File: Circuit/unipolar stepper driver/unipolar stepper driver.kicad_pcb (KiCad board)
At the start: 2 copper layers, 78.7 x 43.2 mm, 20 parts, among them Q1 S8050, Q2 S8050, Q3 S8050, Q4 S8050

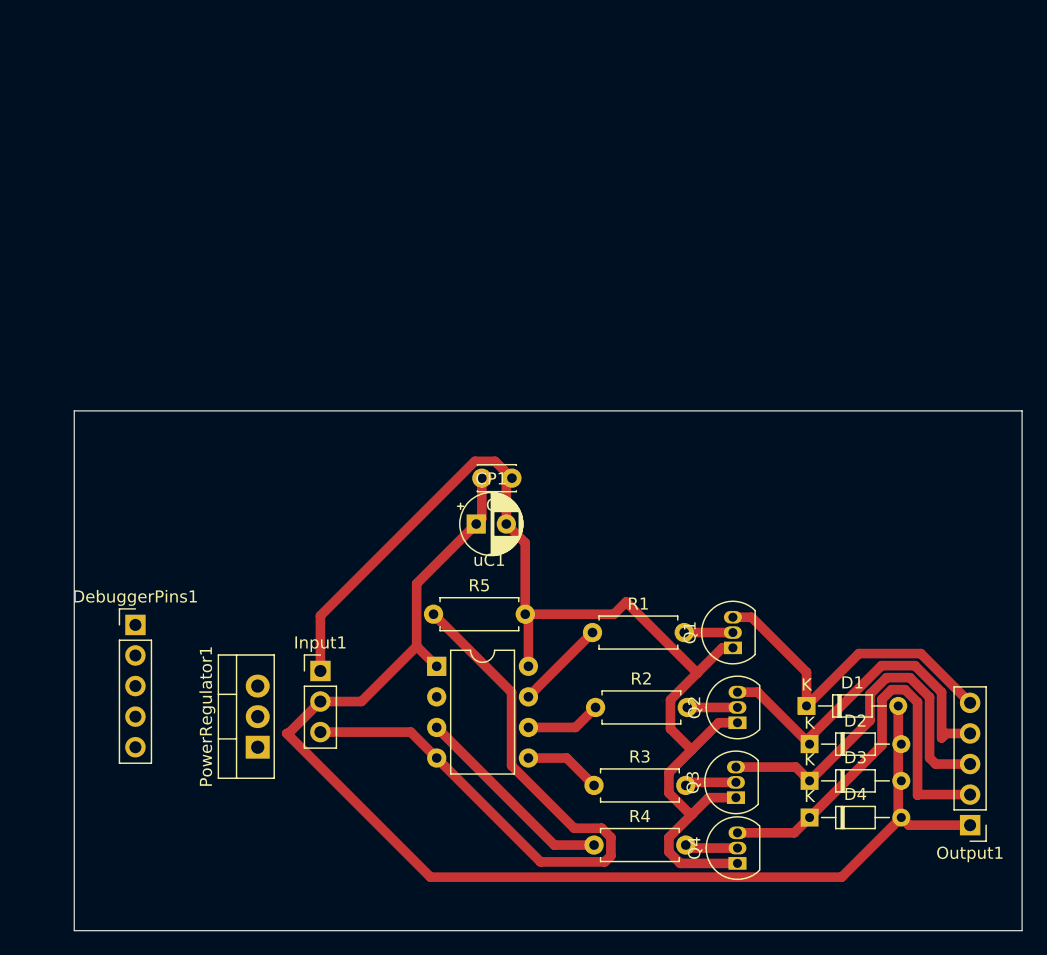
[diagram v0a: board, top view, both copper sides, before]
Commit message: Created Unipolar Stepper PCB design
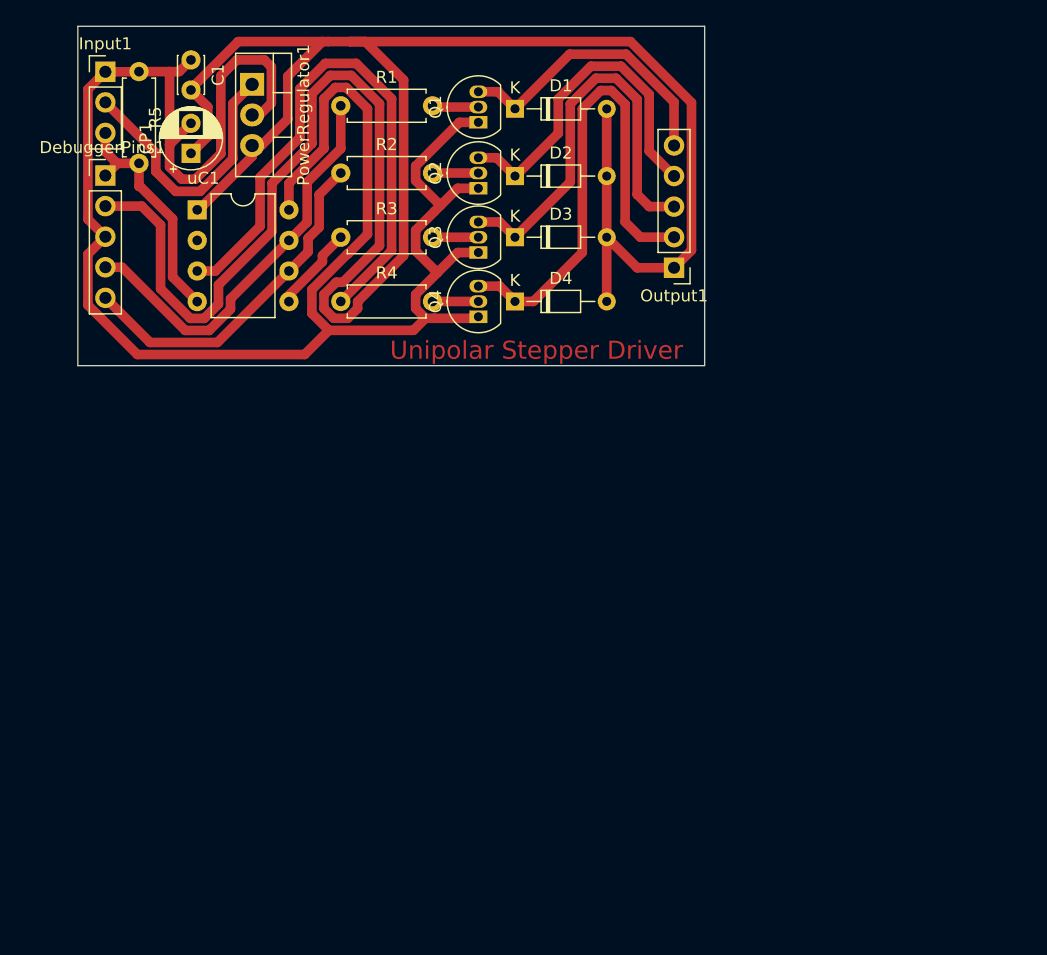
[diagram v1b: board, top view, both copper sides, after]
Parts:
- moved D1 55.2 mm to (49.0, -12.4)
- moved PowerRegulator1 55.1 mm to (27.2, -14.5), turned to -90 degrees
- moved D2 53.2 mm to (49.0, -6.86)
- moved Input1 52.9 mm to (15.0, -15.5)
- moved Output1 52.4 mm to (62.2, 0.76)
- moved D3 51.4 mm to (49.0, -1.78)
- moved R5 51.3 mm to (17.8, -15.5), turned to -90 degrees
- moved Q4 50.3 mm to (46.0, 4.83)
- moved R3 50.2 mm to (34.5, -1.78)
- moved Q3 50.1 mm to (46.0, -0.51)
- moved R4 49.8 mm to (34.5, 3.56)
- moved D4 49.4 mm to (49.0, 3.56)
- moved Q2 49.3 mm to (46.0, -5.84)
- moved R2 49.2 mm to (34.5, -7.11)
- moved Q1 48.5 mm to (46.0, -11.3)
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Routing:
- net +5V: track 105.8 -> 201.1 mm
- net GND: track 98.3 -> 163.5 mm
- net Control_Input: track 56.3 -> 19.7 mm
- net Coil_4: track 17.1 -> 47.8 mm
- net Coil_1: track 7.55 -> 34.0 mm
- net Coil_2: track 6.27 -> 29.2 mm
- net +12V: track 0.00 -> 22.5 mm
- net Net-(D4-Pad1): track 34.7 -> 41.8 mm
- net Net-(D3-Pad1): track 31.0 -> 35.1 mm
- net Net-(D1-Pad1): track 27.9 -> 24.0 mm
- net Coil_3: track 6.39 -> 7.13 mm
- net Net-(Q4-Pad2): track 4.40 -> 3.81 mm
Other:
- board size 78.7 x 43.2 mm -> 52.1 x 28.2 mm
- board text added: "Unipolar Stepper Driver"

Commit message: Fixed numerous bugs in CAM module and marked numerous others
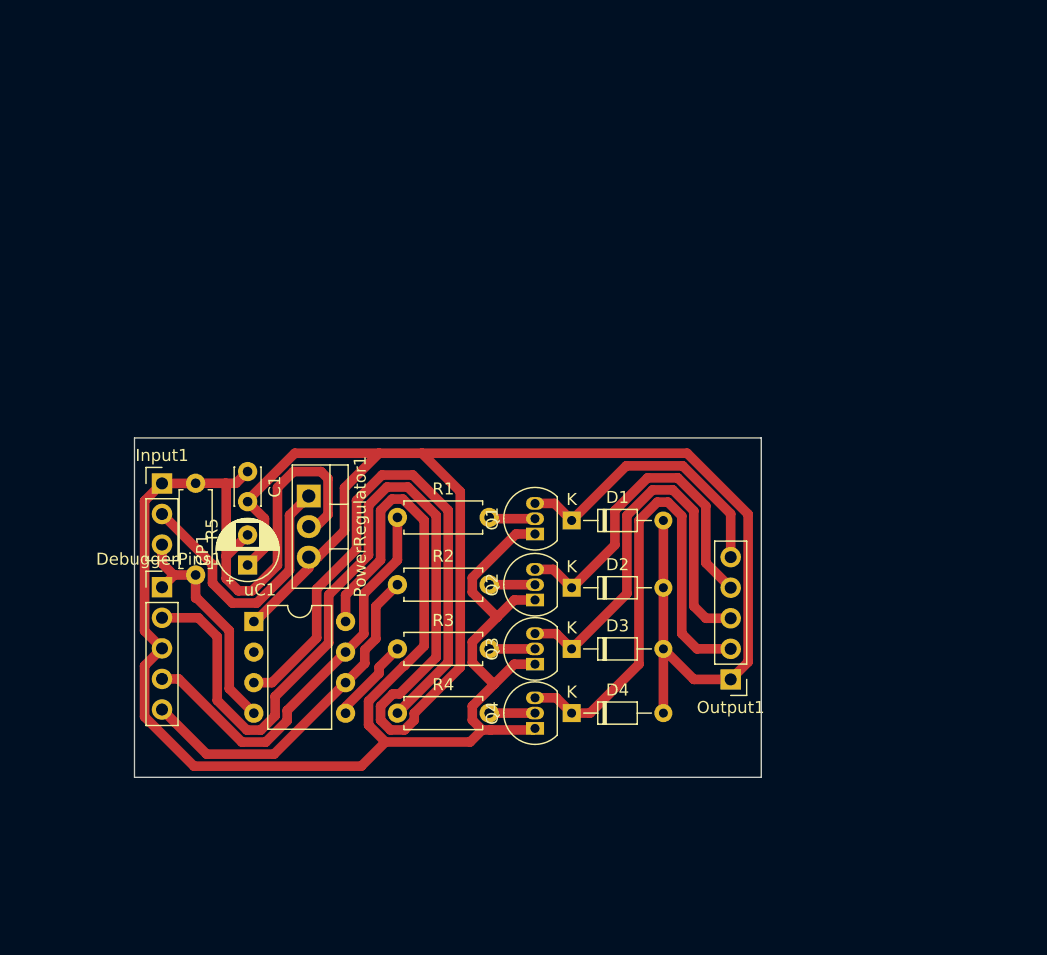
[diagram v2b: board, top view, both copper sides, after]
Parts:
- moved D4 34.5 mm to (53.7, 37.8)
- moved DebuggerPins1 34.5 mm to (19.7, 27.3)
- moved Output1 34.5 mm to (66.9, 35.0)
- moved Q1 34.5 mm to (50.7, 22.9)
- moved Q2 34.5 mm to (50.7, 28.4)
- moved Q3 34.5 mm to (50.7, 33.7)
- moved R2 34.5 mm to (39.2, 27.1)
- moved R4 34.5 mm to (39.2, 37.8)
- moved uC1 34.5 mm to (27.3, 30.1)
- moved C1 34.5 mm to (26.8, 17.7)
- moved CP1 34.5 mm to (26.8, 25.5)
- moved D1 34.5 mm to (53.7, 21.8)
- moved D2 34.5 mm to (53.7, 27.3)
- moved D3 34.5 mm to (53.7, 32.4)
- moved Input1 34.5 mm to (19.7, 18.7)
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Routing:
- net +5V: track 201.1 -> 199.9 mm
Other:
- board text removed: "Unipolar Stepper Driver"

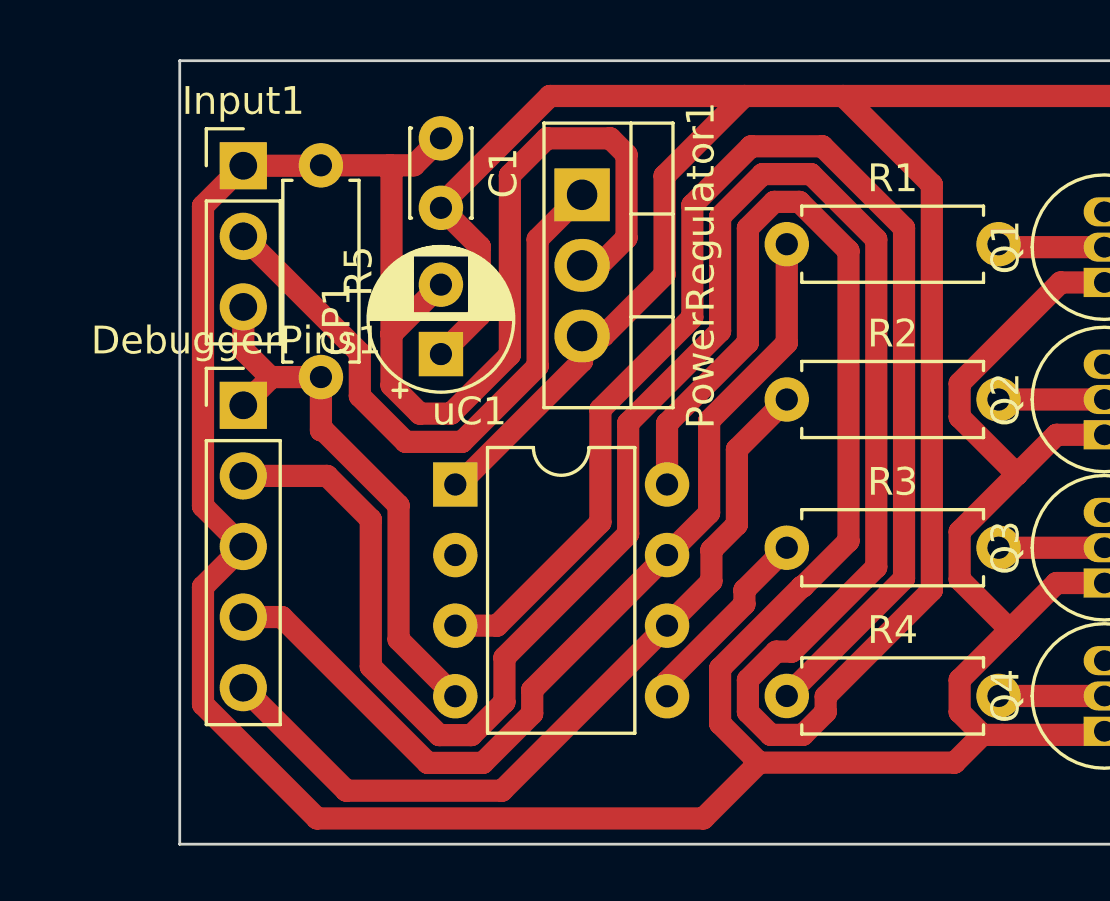
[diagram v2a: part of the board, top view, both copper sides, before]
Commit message: unipolar circuit development
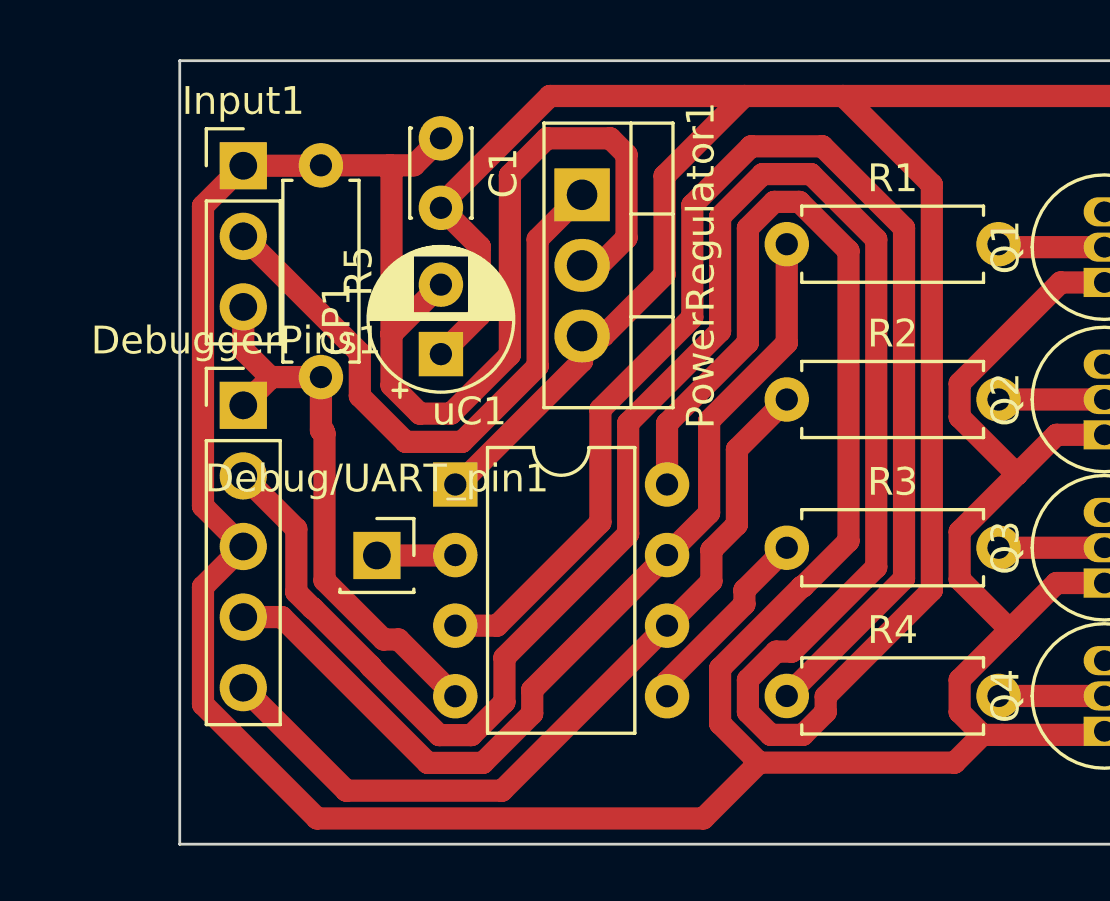
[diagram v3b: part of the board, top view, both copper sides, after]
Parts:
- added Debug/UART_pin1: Conn_01x01_Socket, Connector_PinSocket_2.54mm:PinSocket_1x01_P2.54mm_Vertical, F.Cu at (24.5, 32.7)
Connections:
- uC1 pad 2: unconnected-(uC1-Pad2) -> Debug/UART pin
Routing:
- net Debug/UART pin: track 0.00 -> 2.83 mm
- net +5V: track 199.9 -> 198.9 mm

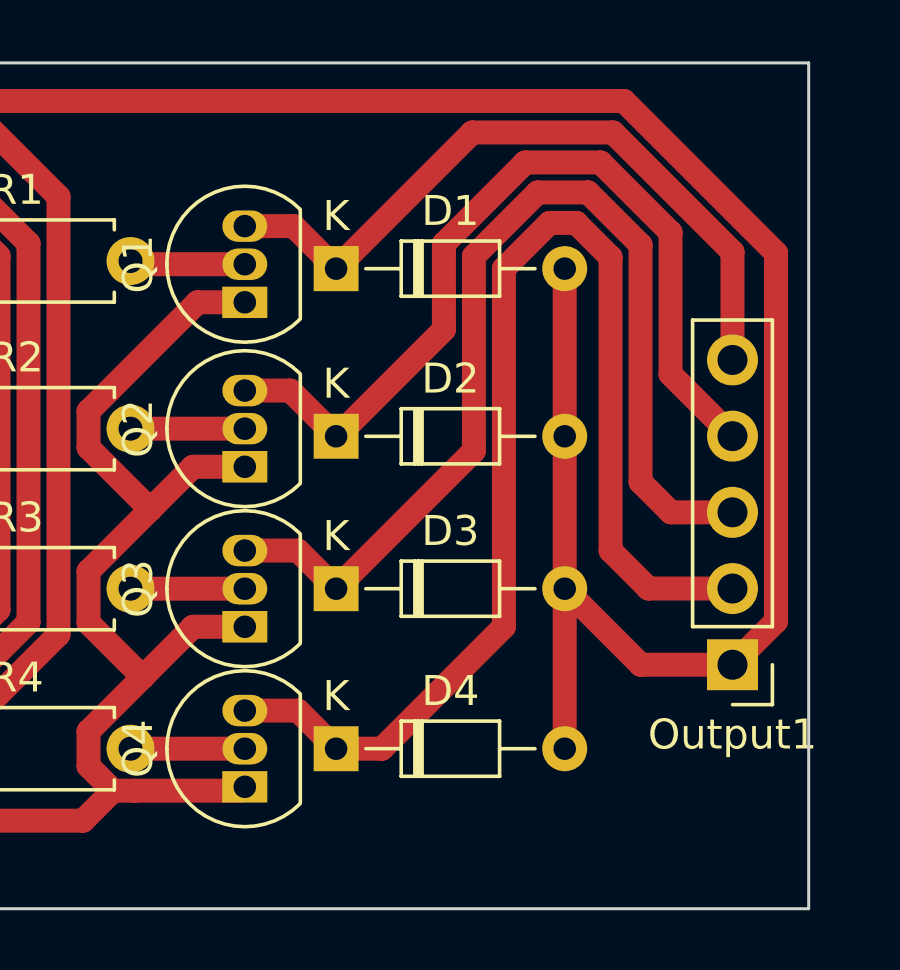
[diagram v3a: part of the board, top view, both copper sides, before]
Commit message: Fixed diode directions in unipolar_driver circuit
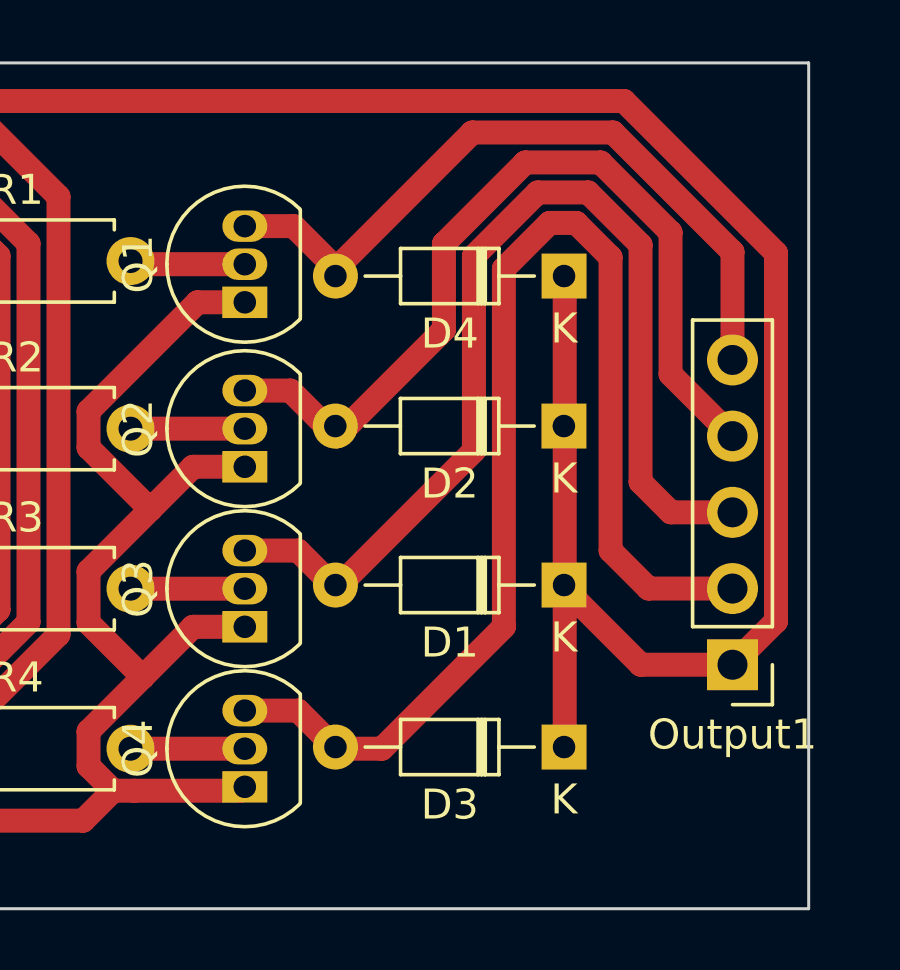
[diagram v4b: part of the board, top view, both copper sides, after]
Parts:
- D1, D2, D3, D4: value DIODE -> 1N5817
- R1, R2: value 300 -> 330
- moved D4 17.5 mm to (61.3, 22.0), turned to 180 degrees
- moved D1 13.0 mm to (61.3, 32.3), turned to 180 degrees
- moved D3 9.25 mm to (61.3, 37.7), turned to 180 degrees
- moved D2 7.60 mm to (61.3, 27.0), turned to 180 degrees
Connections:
- D1 pad 1: Net-(D1-K) -> +5V
- D1 pad 2: +5V -> Net-(D1-A)
- D2 pad 1: Net-(D2-K) -> +5V
- D2 pad 2: +5V -> Net-(D2-A)
- D3 pad 1: Net-(D3-K) -> +5V
- D3 pad 2: +5V -> Net-(D3-A)
- D4 pad 1: Net-(D4-K) -> +5V
- D4 pad 2: +5V -> Net-(D4-A)
- Output1 pad 2: Net-(D4-K) -> Net-(D3-A)
- Output1 pad 3: Net-(D3-K) -> Net-(D1-A)
- Output1 pad 4: Net-(D2-K) -> Net-(D2-A)
- Output1 pad 5: Net-(D1-K) -> Net-(D4-A)
- Q1 pad 3: Net-(D1-K) -> Net-(D4-A)
- Q2 pad 3: Net-(D2-K) -> Net-(D2-A)
- Q3 pad 3: Net-(D3-K) -> Net-(D1-A)
- Q4 pad 3: Net-(D4-K) -> Net-(D3-A)
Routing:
- net Net-(D4-K): track 41.8 -> 0.00 mm
- net Net-(D3-A): track 0.00 -> 41.8 mm
- net Net-(D3-K): track 35.1 -> 0.00 mm
- net Net-(D1-A): track 0.00 -> 35.1 mm
- net Net-(D2-K): track 28.9 -> 0.00 mm
- net Net-(D2-A): track 0.00 -> 28.9 mm
- net Net-(D4-A): track 0.00 -> 24.0 mm
- net Net-(D1-K): track 24.0 -> 0.00 mm
